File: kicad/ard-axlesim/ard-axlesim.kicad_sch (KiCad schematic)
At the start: 23 parts, among them J1 Power, J10 SM04B-SRSS, J2 Digital/PWM, J3 Analog, J4 Digital/PWM, J5 Conn_01x03, J6 Conn_01x03, J7 Conn_01x03, J8 Conn_01x03, J9 SM04B-SRSS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

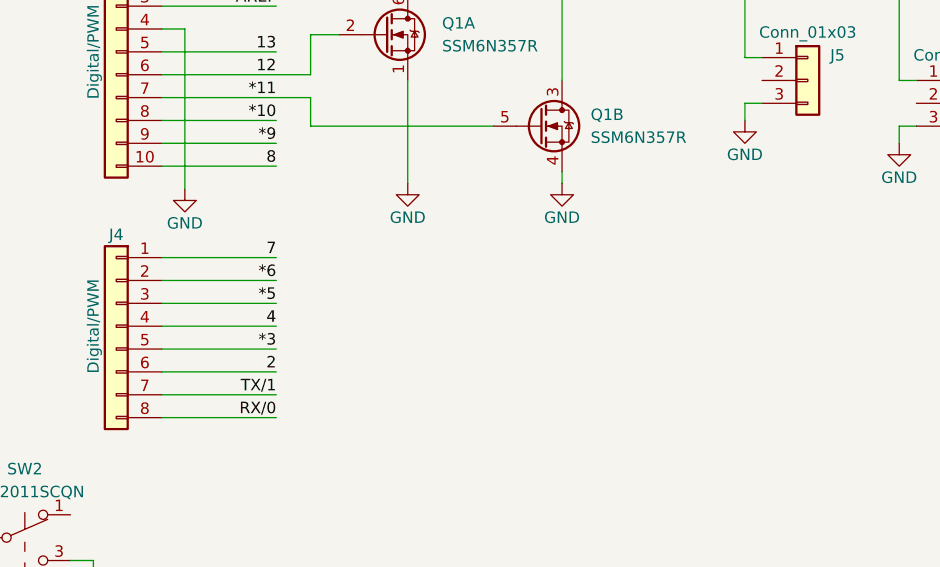
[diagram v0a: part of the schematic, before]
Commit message: Added DIP switch
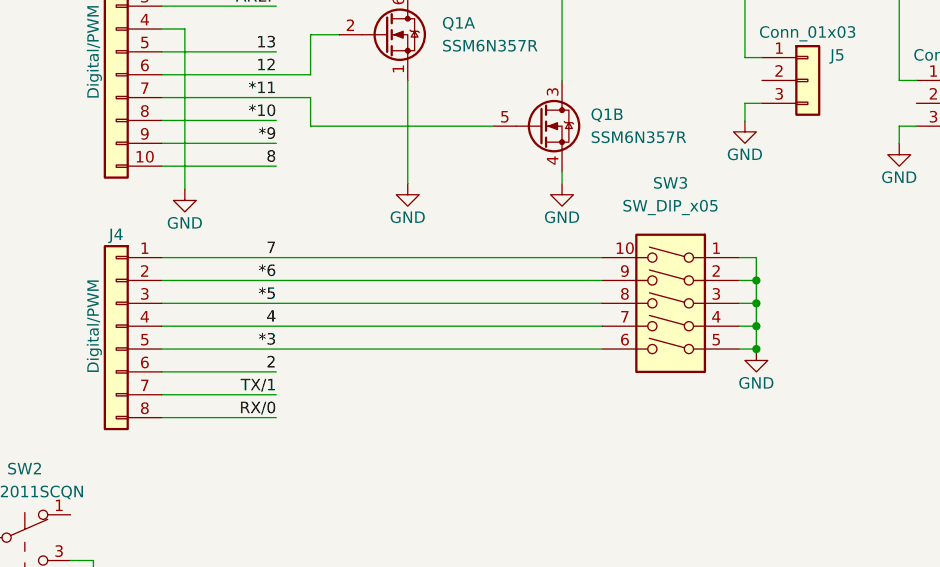
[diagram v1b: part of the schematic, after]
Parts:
- added SW3: SW_DIP_x05, ISE_UltraLibrarian:CST_219SMT, symbol Switch:SW_DIP_x05
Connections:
- net *3: now also SW3.6
- net *5: now also SW3.8
- net *6: now also SW3.9
- net 4: now also SW3.7
- net 7: now also SW3.10
- net GND: now also SW3.1, SW3.2, SW3.3, SW3.4, SW3.5

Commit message: Updates after review
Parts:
- added C3: 0.1uF, Capacitor_SMD:C_0805_2012Metric, symbol Device:C
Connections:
- net +3.3V is gone; now on net +5V: J10.2 (Pin_2), J9.2 (Pin_2), R1.2, R2.2, R3.2, R4.2
- net +5V: no longer J1.5 (Pin_5)
- net GND: now also C3.2
- net SCL/A5: now also C3.1
- net at SW2.1 (A): now also SW2.4 (A)
- net +3V3 renamed ARD_3V3
- new net ARD_5V: J1.5 (Pin_5)
